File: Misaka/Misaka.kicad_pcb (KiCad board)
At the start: 2 copper layers, 100 x 86.6 mm, 106 parts, among them J1 Conn_Coaxial_Power, J2 Conn_01x04_Male, J3 Conn_01x04_Male, J4 Conn_01x04_Male, J5 USB_B_Micro, J6 Conn_01x04_Female, J7 Conn_01x04_Female_UART, J8 Conn_02x04_Odd_Even, J9 Conn_01x07, SW1 SW_DIP_x03, U1 DRV8825PWPR, U2 ATmega2560-16AU, U3 DRV8825PWPR, U4 DRV8825PWPR, U5 CH340C, U6 AMS1117-5.0, U7 AMS1117-3.3, U8 24LC02, Y1 CSTLS16M0X51-B0

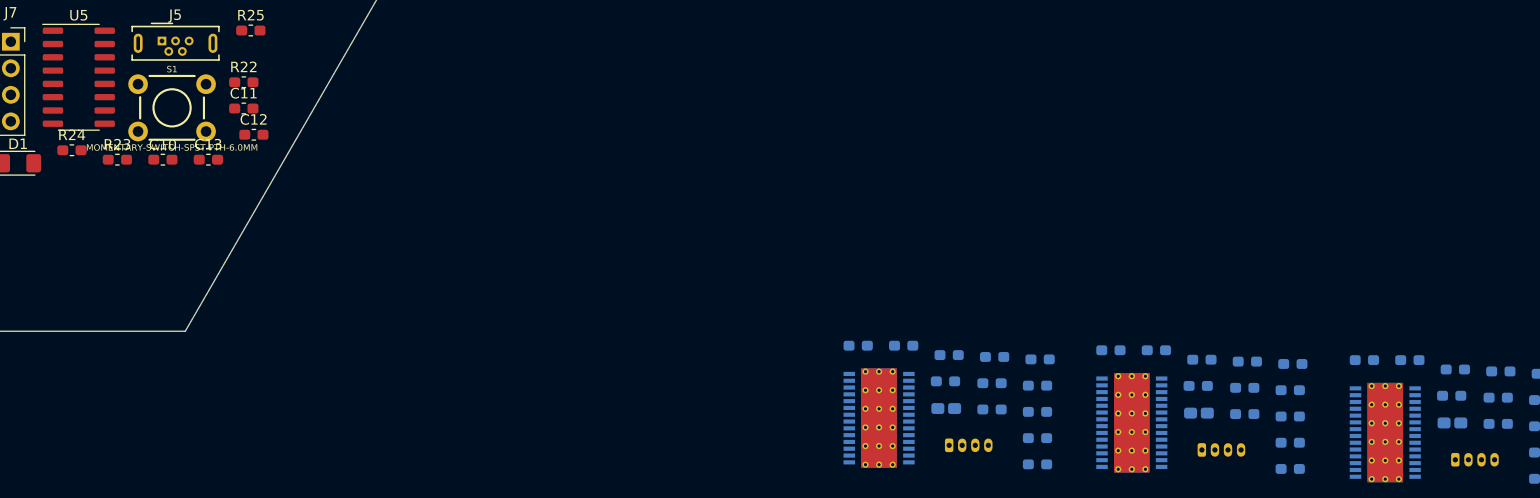
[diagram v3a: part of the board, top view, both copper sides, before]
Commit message: Change Footprint
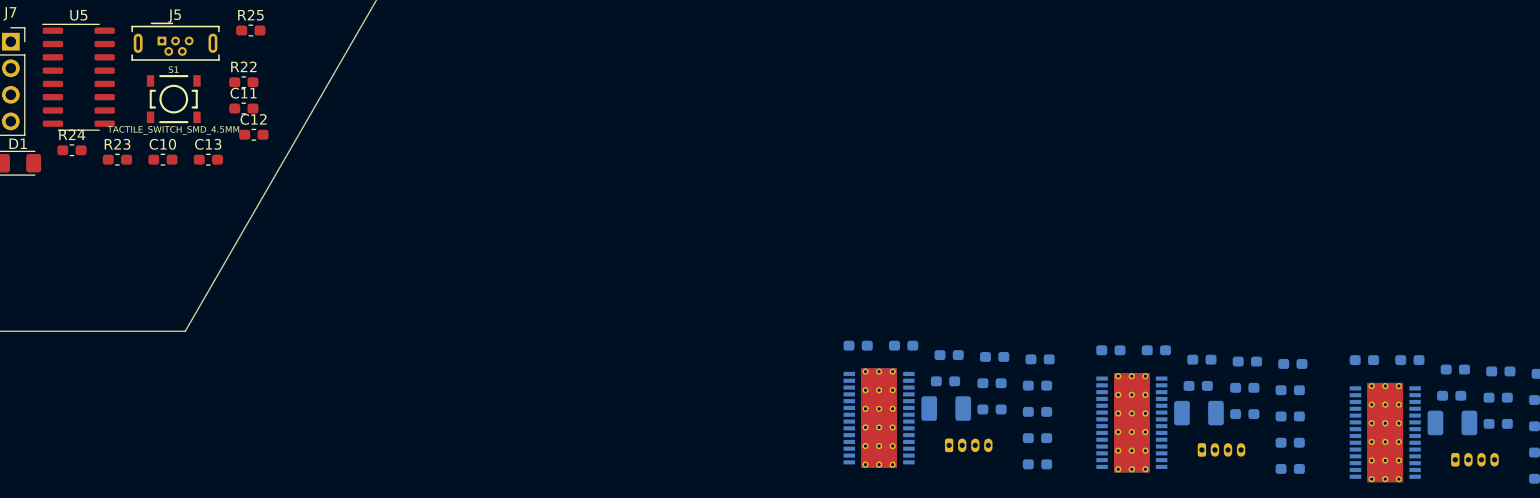
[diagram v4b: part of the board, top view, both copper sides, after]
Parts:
- CP1, CP2, CP3: footprint Capacitor_Tantalum_SMD:CP_EIA-1608-08_AVX-J_Pad1.25x1.05mm_HandSolder -> Capacitor_Tantalum_SMD:CP_EIA-3528-21_Kemet-B_Pad1.50x2.35mm_HandSolder
- S1: value MOMENTARY-SWITCH-SPST-PTH-6.0MM -> TACTILE_SWITCH_SMD_4.5MM; footprint Switches:TACTILE_SWITCH_PTH_6.0MM -> Switches:TACTILE_SWITCH_SMD_4.5MM
- moved S1 0.85 mm to (98.9, 96.1)
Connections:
- D10 pad 2: Net-(D10-Pad2) -> (no net)
- J5 pad 4: Net-(J5-Pad4) -> (no net)
- J8 pad 6: Net-(J8-Pad6) -> (no net)
- MOD1 pad 11: Net-(MOD1-Pad11) -> (no net)
- MOD1 pad 12: Net-(MOD1-Pad12) -> (no net)
- MOD1 pad 13: Net-(MOD1-Pad13) -> (no net)
- MOD1 pad 14: Net-(MOD1-Pad14) -> (no net)
- MOD1 pad 15: Net-(MOD1-Pad15) -> (no net)
- MOD1 pad 16: Net-(MOD1-Pad16) -> (no net)
- MOD1 pad 17: Net-(MOD1-Pad17) -> (no net)
- MOD1 pad 18: Net-(MOD1-Pad18) -> (no net)
- MOD1 pad 19: Net-(MOD1-Pad19) -> (no net)
- MOD1 pad 20: Net-(MOD1-Pad20) -> (no net)
- MOD1 pad 4: Net-(MOD1-Pad4) -> (no net)
- MOD1 pad 5: Net-(MOD1-Pad5) -> (no net)
- MOD1 pad 6: Net-(MOD1-Pad6) -> (no net)
- MOD1 pad 7: Net-(MOD1-Pad7) -> (no net)
- MOD1 pad 8: Net-(MOD1-Pad8) -> (no net)
- MOD1 pad 9: Net-(MOD1-Pad9) -> (no net)
- S1 pad 2: (no net) -> GND
- S1 pad 3: GND -> (no net)
- U1 pad 19: Net-(U1-Pad19) -> (no net)
- U1 pad 21: Net-(U1-Pad21) -> (no net)
- U1 pad 23: Net-(U1-Pad23) -> (no net)
- U2 pad 1: Net-(U2-Pad1) -> (no net)
- U2 pad 14: Net-(U2-Pad14) -> (no net)
- U2 pad 19: /D53 -> (no net)
- U2 pad 25: /D12 -> (no net)
- U2 pad 27: Net-(U2-Pad27) -> (no net)
- U2 pad 28: Net-(U2-Pad28) -> (no net)
- U2 pad 29: Net-(U2-Pad29) -> (no net)
- U2 pad 35: Net-(U2-Pad35) -> (no net)
- U2 pad 36: Net-(U2-Pad36) -> (no net)
- U2 pad 37: Net-(U2-Pad37) -> (no net)
- U2 pad 38: Net-(U2-Pad38) -> (no net)
- U2 pad 39: Net-(U2-Pad39) -> (no net)
- U2 pad 4: Net-(U2-Pad4) -> (no net)
- U2 pad 40: Net-(U2-Pad40) -> (no net)
- U2 pad 41: Net-(U2-Pad41) -> (no net)
- U2 pad 42: Net-(U2-Pad42) -> (no net)
- U2 pad 47: Net-(U2-Pad47) -> (no net)
- U2 pad 48: Net-(U2-Pad48) -> (no net)
- U2 pad 49: Net-(U2-Pad49) -> (no net)
- U2 pad 5: Net-(U2-Pad5) -> (no net)
- U2 pad 50: Net-(U2-Pad50) -> (no net)
- U2 pad 51: Net-(U2-Pad51) -> (no net)
- U2 pad 52: Net-(U2-Pad52) -> (no net)
- U2 pad 53: Net-(U2-Pad53) -> (no net)
- U2 pad 54: Net-(U2-Pad54) -> (no net)
- U2 pad 55: Net-(U2-Pad55) -> (no net)
- U2 pad 56: Net-(U2-Pad56) -> (no net)
- U2 pad 57: Net-(U2-Pad57) -> (no net)
- U2 pad 58: Net-(U2-Pad58) -> (no net)
- U2 pad 59: Net-(U2-Pad59) -> (no net)
- U2 pad 6: Net-(U2-Pad6) -> (no net)
- U2 pad 60: Net-(U2-Pad60) -> (no net)
- U2 pad 63: /RX3 -> (no net)
- U2 pad 64: /TX3 -> (no net)
- U2 pad 65: Net-(U2-Pad65) -> (no net)
- U2 pad 66: Net-(U2-Pad66) -> (no net)
- U2 pad 67: Net-(U2-Pad67) -> (no net)
- U2 pad 68: Net-(U2-Pad68) -> (no net)
- U2 pad 69: Net-(U2-Pad69) -> (no net)
- U2 pad 70: Net-(U2-Pad70) -> (no net)
- U2 pad 71: Net-(U2-Pad71) -> (no net)
- U2 pad 72: Net-(U2-Pad72) -> (no net)
- U2 pad 73: Net-(U2-Pad73) -> (no net)
- U2 pad 74: Net-(U2-Pad74) -> (no net)
- U2 pad 75: Net-(U2-Pad75) -> (no net)
- U2 pad 76: Net-(U2-Pad76) -> (no net)
- U2 pad 77: Net-(U2-Pad77) -> (no net)
- U2 pad 78: Net-(U2-Pad78) -> (no net)
- U2 pad 79: Net-(U2-Pad79) -> (no net)
- U2 pad 8: Net-(U2-Pad8) -> (no net)
- U2 pad 82: Net-(U2-Pad82) -> (no net)
- U2 pad 83: Net-(U2-Pad83) -> (no net)
- U2 pad 84: Net-(U2-Pad84) -> (no net)
- U2 pad 85: Net-(U2-Pad85) -> (no net)
- U2 pad 86: Net-(U2-Pad86) -> (no net)
- U2 pad 87: Net-(U2-Pad87) -> (no net)
- U2 pad 88: Net-(U2-Pad88) -> (no net)
- U2 pad 89: Net-(U2-Pad89) -> (no net)
- U2 pad 9: Net-(U2-Pad9) -> (no net)
- U2 pad 90: Net-(U2-Pad90) -> (no net)
- U2 pad 91: Net-(U2-Pad91) -> (no net)
- U2 pad 92: Net-(U2-Pad92) -> (no net)
- U2 pad 93: Net-(U2-Pad93) -> (no net)
- U2 pad 94: Net-(U2-Pad94) -> (no net)
- U2 pad 95: Net-(U2-Pad95) -> (no net)
- U2 pad 96: Net-(U2-Pad96) -> (no net)
- U2 pad 97: Net-(U2-Pad97) -> (no net)
- U2 pad 98: Net-(U2-Pad98) -> (no net)
- U3 pad 19: Net-(U3-Pad19) -> (no net)
- U3 pad 21: Net-(U3-Pad21) -> (no net)
- U3 pad 23: Net-(U3-Pad23) -> (no net)
- U4 pad 19: Net-(U4-Pad19) -> (no net)
- U4 pad 21: Net-(U4-Pad21) -> (no net)
- U4 pad 23: Net-(U4-Pad23) -> (no net)
- U5 pad 10: Net-(U5-Pad10) -> (no net)
- U5 pad 11: Net-(U5-Pad11) -> (no net)
- U5 pad 12: Net-(U5-Pad12) -> (no net)
- U5 pad 14: Net-(U5-Pad14) -> (no net)
- U5 pad 15: Net-(U5-Pad15) -> (no net)
- U5 pad 7: Net-(U5-Pad7) -> (no net)
- U5 pad 8: Net-(U5-Pad8) -> (no net)
- U5 pad 9: Net-(U5-Pad9) -> (no net)

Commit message: route v2.2
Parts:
- removed LED1: ON, LED_SMD:LED_0603_1608Metric_Pad1.05x0.95mm_HandSolder
- removed R27: 1k, Resistor_SMD:R_0603_1608Metric_Pad1.05x0.95mm_HandSolder
- SW1: moved to B.Cu
- moved R19 157.8 mm to (80.0, 78.2)
- moved C-VMB2 152.7 mm to (81.5, 37.6)
- moved R16 152.1 mm to (86.1, 80.3)
- moved C-VMB3 151.4 mm to (81.5, 93.7), turned to 90 degrees
- moved R9 149.6 mm to (89.2, 37.6)
- moved C-VMA3 149.2 mm to (88.1, 78.5), turned to 180 degrees
- moved J4 146.6 mm to (82.5, 83.9), turned to 270 degrees
- moved R3 145.4 mm to (40.5, 93.3), turned to 180 degrees
- moved R12 144.8 mm to (82.0, 44.2)
- moved R18 144.3 mm to (83.8, 78.5)
- moved R13 142.9 mm to (94.5, 39.1), turned to 180 degrees
- moved R17 142.2 mm to (86.6, 94.5)
- moved J3 141.8 mm to (81.3, 48.0), turned to 270 degrees
- moved R11 141.2 mm to (82.0, 41.4)
- moved R15 140.9 mm to (94.5, 75.4), turned to 180 degrees
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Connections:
- S1 pad 1: /RESET -> GND
- S1 pad 2: GND -> /RESET
- S1 pad 3: (no net) -> /RESET
- S1 pad 4: (no net) -> GND
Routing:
- net +5V: track 0.00 -> 436.0 mm, vias 0 -> 9
- net +12V: track 0.00 -> 253.0 mm, vias 0 -> 7
- net +3V3: track 0.00 -> 162.2 mm, vias 0 -> 4
- net /MS3: track 0.00 -> 138.4 mm, vias 0 -> 9
- net /MS2: track 0.00 -> 132.7 mm, vias 0 -> 8
- net /MS1: track 0.00 -> 121.8 mm, vias 0 -> 7
- net /D3: track 0.00 -> 89.5 mm, vias 0 -> 2
- net /D10: track 0.00 -> 82.6 mm, vias 0 -> 3
- net /RESET: track 0.00 -> 76.7 mm, vias 0 -> 3
- net /D9: track 0.00 -> 69.9 mm, vias 0 -> 3
- net /D11: track 0.00 -> 69.8 mm, vias 0 -> 3
- net /D8: track 0.00 -> 66.9 mm, vias 0 -> 3
- net /RX1: track 0.00 -> 49.6 mm
- net /TX1: track 0.00 -> 47.4 mm
- net /SCL: track 0.00 -> 45.4 mm, vias 0 -> 2
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
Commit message: v2 finish
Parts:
- moved U8 0.72 mm to (79.6, 67.6)
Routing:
- net GND: track 36.9 -> 647.0 mm, vias 0 -> 29
- net +12V: track 253.0 -> 285.8 mm, vias 7 -> 11
- net +5V: track 436.0 -> 463.2 mm, vias 9 -> 12
- net +3V3: track 162.2 -> 171.9 mm
- net /CameraModule/E2PROM-SCK: track 33.5 -> 36.0 mm, vias 0 -> 1
- net /CameraModule/E2PROM-SDA: track 32.3 -> 33.8 mm
- net Net-(R2-Pad2): track 16.7 -> 17.9 mm
- net Net-(R32-Pad2): track 3.99 -> 4.85 mm
- net Net-(R15-Pad2): track 16.6 -> 17.4 mm
- added copper zone on B.Cu, net GND
- added copper zone on F.Cu, net GND
